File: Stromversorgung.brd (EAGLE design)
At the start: 70 x 100 mm, 17 parts, among them IC1 LM2574N-3.3, X1 MSTBV4, X2 Power ext., 5V 1A, X4 Power int., 5V 3A

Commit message: Pi und Stromversorgung Rev. 2019
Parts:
- removed C1: 22µF 75V, rcl:E2,5-5
- removed C2: 220µF 25V, rcl:E2,5-5
- removed D1: 1N5819-B, diode:DO41-7.6
- removed IC1: LM2574N-3.3, linear:DIL08
- removed L1: 100µH, rcl:6000-XXXX-RC
- removed SV1: PLATINENVERBINDER-31SMD, homepi:PLATINENVERBINDER-31-SMD
- removed X4: Power int., 5V 3A, con-phoenix-508:MSTBV2
- added J1: DCJ0202, con-jack:DCJ0202
- added U1, U3: TSR_2-2450, _traco_tsr-1:TSR-1
- added U2: TSR_0.5-2433, _traco_tsr-1:TSR-1
- X1: value MSTBV4 -> Ein/Aus; device con-phoenix-508:MSTBV4 -> con-phoenix-508:MSTBV2
- X2: value Power ext., 5V 1A -> MAC64L; device con-phoenix-508:MSTBV2 -> con-vg:MAC64L
- moved X2 65.0 mm to (2.54, 50.0), turned to 180 degrees
- moved R2 50.8 mm to (53.3, 63.5)
- moved JP2 45.6 mm to (45.7, 63.5), turned to 90 degrees
- moved LED2 43.2 mm to (59.7, 62.2), turned to 270 degrees
- moved R1 38.1 mm to (53.3, 47.0)
- moved LED1 35.6 mm to (59.7, 45.7), turned to 270 degrees
- moved X1 31.1 mm to (58.4, 28.6)
- moved JP1 23.3 mm to (45.7, 58.4), turned to 270 degrees
- moved LED3 16.6 mm to (59.7, 77.5), turned to 270 degrees
- moved R3 14.0 mm to (53.3, 78.7)
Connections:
- removed net +3,3V_INT_1: C2.+, IC1.1, JP2.2, L1.1
- removed net GND_EXT: LED3.K, SV1.30, SV1.30T, X2.1
- removed net GND_INT: C1.-, C2.-, D1.A, IC1.2, IC1.3, IC1.4, LED1.K, LED2.K, SV1.29, SV1.29T, SV1.3, SV1.3T, SV1.6, SV1.6T, SV1.8, SV1.8T, X4.1
- removed net LM2574_IN: C1.+, IC1.5, JP1.1
- removed net LM2574_OUT: D1.C, IC1.7, L1.2
- removed net N$3: X1.3, X4.2
- new net +24V: JP1.2, U1.1, U3.1, X1.1, X2.A32, X2.C32
- new net GND: J1.3, LED1.K, LED2.K, LED3.K, U1.2, U2.2, U3.2, X2.A29, X2.A3, X2.A30, X2.A6, X2.A8, X2.C29, X2.C3, X2.C30, X2.C6, X2.C8
- new net N$2: JP2.2, U2.3
- new net VI: JP1.1, U2.1
- net +3,3V: now also X2.A2, X2.C2; no longer SV1.2, SV1.2T
- net +5V_EXT: now also U3.3, X2.A31, X2.C31; no longer SV1.31, SV1.31T, X1.2
- net +5V_INT: now also U1.3, X2.A1, X2.A28, X2.C1, X2.C28; no longer JP1.2, SV1.1, SV1.1T, SV1.28, SV1.28T, X1.4
- net N$1: now also J1.1, X1.2; no longer X1.1, X2.2
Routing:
- net GND: track 0.00 -> 309.6 mm
- net GND_INT: track 179.1 -> 0.00 mm
- net +24V: track 0.00 -> 141.2 mm
- net N$4: track 102.9 -> 0.00 mm
- net +5V_INT: track 229.0 -> 148.9 mm, vias 2 -> 1
- net GND_EXT: track 73.1 -> 0.00 mm
- net +5V_EXT: track 108.1 -> 53.8 mm, vias 1 -> 0
- net +3,3V: track 51.6 -> 92.8 mm
- net N$3: track 31.6 -> 0.00 mm
- net LM2574_IN: track 18.8 -> 0.00 mm
- net N$7: track 6.66 -> 0.00 mm
- net VI: track 0.00 -> 6.35 mm
- net N$2: track 0.00 -> 6.35 mm
- net N$1: track 19.5 -> 20.6 mm
- added copper zone on layer 16, net GND
- removed copper zone on layer 16, net +3,3V_INT_1
- removed copper zone on layer 16, net GND_INT
- removed copper zone on layer 16, net LM2574_OUT
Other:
- board text added: "+24V Eingang"
- board text added: "+3,3V"
- board text added: "HomePi Stromversorgung Rev 2019/03 (c) Peter Müller"
- board text removed: "+3,3V i.O."
- board text removed: "+5V i.O."
- board text removed: "Erzeug. +3,3V"
- board text removed: "HomePi Stromversorgung Rev 2015/12 (c) Peter Müller"

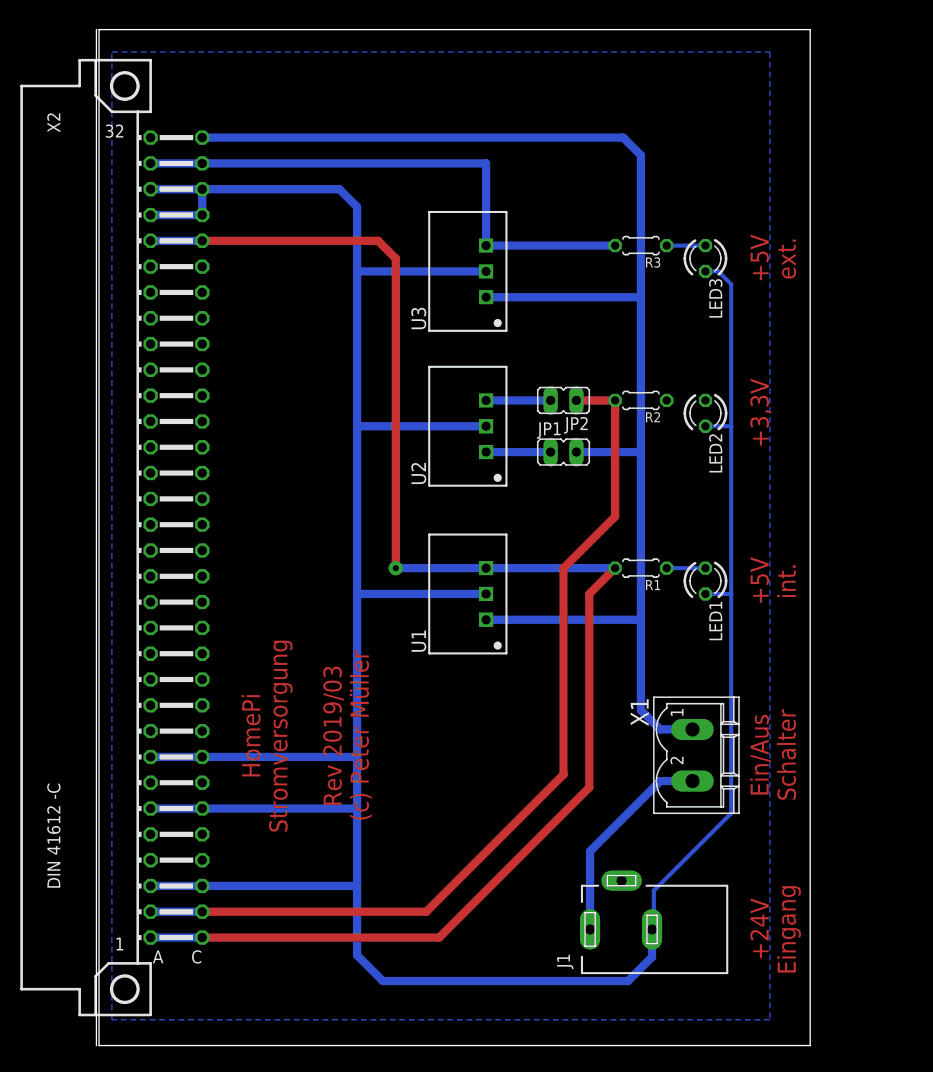
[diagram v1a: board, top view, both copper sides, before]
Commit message: Anpassungen an Rev. 2019, erste Can-Bus Elemente
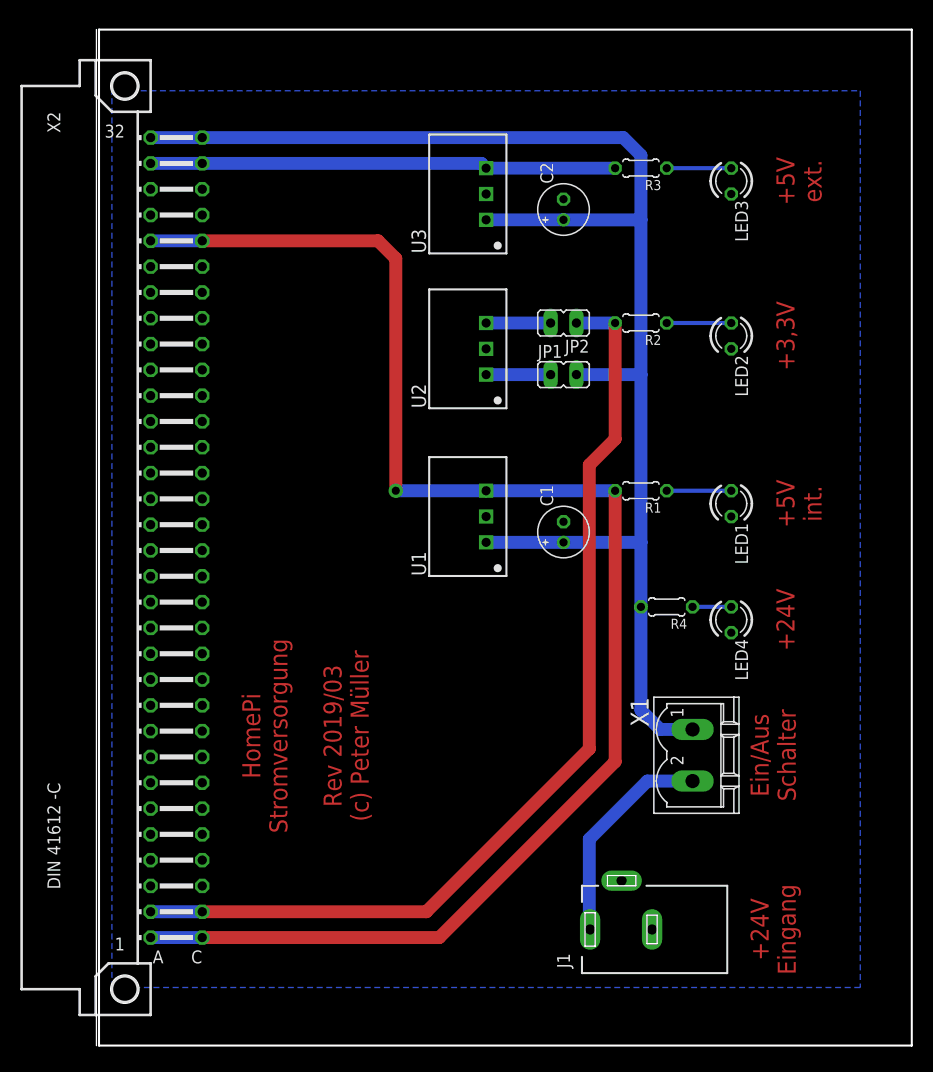
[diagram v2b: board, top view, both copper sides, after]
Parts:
- added C1, C2: 22µF/50V, rcl:E2-5
- added LED4: 2mA ge, led:LED3MM
- added R4: 12k, rcl:0204/5
- U1, U3: value TSR_2-2450 -> TSR 2-2450
- U2: value TSR_0.5-2433 -> TSR 1-2433
- moved LED1 8.03 mm to (62.2, 53.3)
- moved LED3 8.03 mm to (62.2, 85.1)
- moved LED2 8.03 mm to (62.2, 69.8)
- moved JP1 7.62 mm to (45.7, 66.0)
- moved JP2 7.62 mm to (45.7, 71.1)
- moved R2 7.62 mm to (53.3, 71.1)
- moved R3 7.62 mm to (53.3, 86.4)
- moved R1 7.62 mm to (53.3, 54.6)
- moved U1 7.62 mm to (38.1, 52.1)
- moved U2 7.62 mm to (38.1, 68.6)
- moved U3 7.62 mm to (38.1, 83.8)
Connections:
- new net N$3: LED4.A, R4.1
- net +24V: now also C1.+, C2.+, R4.2
- net GND: now also C1.-, C2.-, LED4.K
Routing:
- net GND: track 309.6 -> 0.00 mm
- net +5V_EXT: track 53.8 -> 45.9 mm
- net N$7: track 0.00 -> 6.35 mm
- net +24V: track 141.2 -> 146.3 mm
- net +3,3V: track 92.8 -> 96.6 mm
- net N$3: track 0.00 -> 3.81 mm
- net N$8: track 3.81 -> 6.35 mm
- net N$6: track 3.81 -> 6.35 mm
- net N$1: track 20.6 -> 21.4 mm
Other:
- board size 70 x 100 mm -> 80 x 100 mm
- board text added: "+24V"

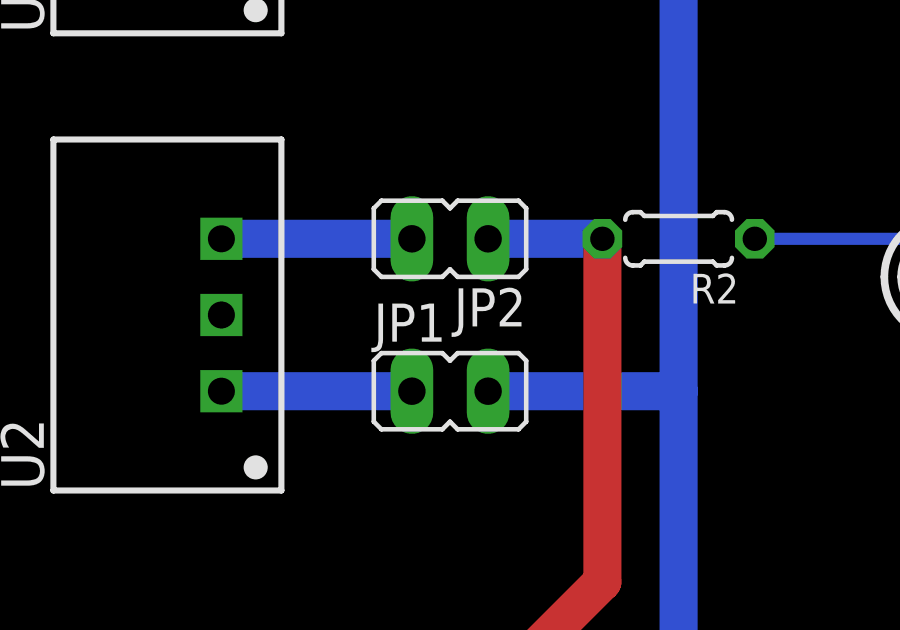
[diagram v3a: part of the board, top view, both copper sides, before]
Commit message: 3,3V-Versorgung nur noch über TSR-Spannungsregler
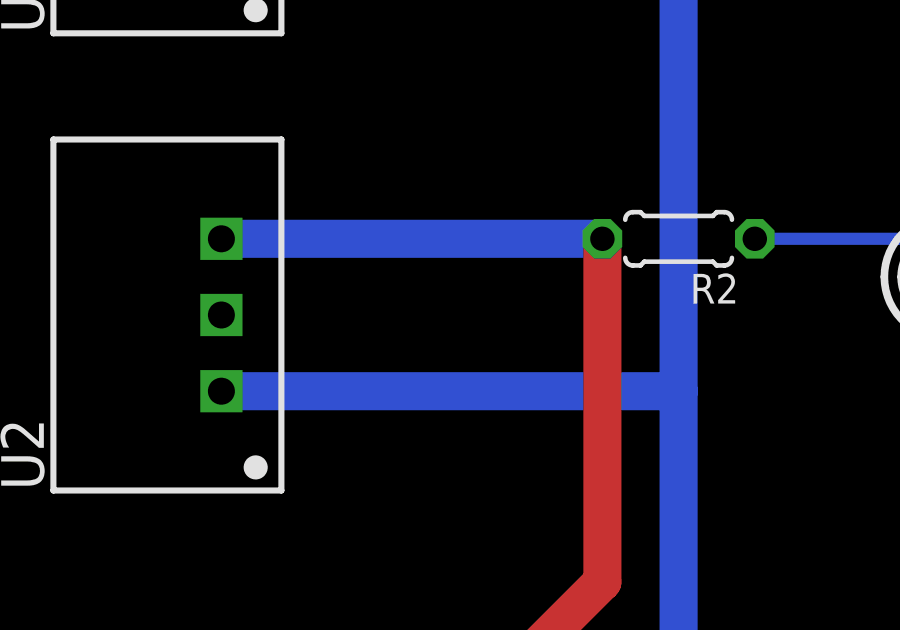
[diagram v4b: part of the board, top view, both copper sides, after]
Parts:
- removed JP1, JP2: (no value), jumper:JP1
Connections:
- removed net N$2: JP2.2, U2.3
- removed net VI: JP1.1, U2.1
- net +24V: now also U2.1; no longer JP1.2
- net +3,3V: now also U2.3; no longer JP2.1
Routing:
- net +3,3V: track 96.6 -> 105.5 mm
- net +24V: track 146.3 -> 155.2 mm
- net VI: track 6.35 -> 0.00 mm
- net N$2: track 6.35 -> 0.00 mm
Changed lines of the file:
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@@
 </autorouter>
 <elements>
-<element name="JP1" library="jumper" package="JP1" value="" x="45.72" y="66.04" rot="R270"/>
-<element name="JP2" library="jumper" package="JP1" value="" x="45.72" y="71.12" rot="R90"/>
 <element name="X1" library="con-phoenix-508" package="MSTBV2" value="Ein/Aus" x="58.42" y="28.575" rot="R270">
 <attribute name="OC_NEWARK" value="69R9845" x="58.42" y="28.575" size="1.778" layer="27" rot="R270" display="off"/>
@@
 </signal>
 <signal name="+3,3V">
-<contactref element="JP2" pad="1"/>
 <contactref element="R2" pad="2"/>
 <contactref element="X2" pad="A2"/>
@@
 <wire x1="48.26" y1="57.15" x2="48.26" y2="29.21" width="1.27" layer="1"/>
 <wire x1="10.16" y1="13.17" x2="5.08" y2="13.17" width="1.27" layer="16"/>
-<wire x1="46.99" y1="71.12" x2="50.8" y2="71.12" width="1.27" layer="16"/>
+<contactref element="U2" pad="3"/>
+<wire x1="38.1" y1="71.12" x2="50.8" y2="71.12" width="1.27" layer="16"/>
 </signal>
 <signal name="N$6">
@@
 <signal name="N$4">
 </signal>
-<signal name="N$2">
-<contactref element="U2" pad="3"/>
-<contactref element="JP2" pad="2"/>
-<wire x1="44.45" y1="71.12" x2="38.1" y2="71.12" width="1.27" layer="16"/>
-</signal>
-<signal name="VI">
-<contactref element="JP1" pad="1"/>
-<contactref element="U2" pad="1"/>
-<wire x1="44.45" y1="66.04" x2="38.1" y2="66.04" width="1.27" layer="16"/>
-</signal>
 <signal name="+24V">
-<contactref element="JP1" pad="2"/>
 <contactref element="U1" pad="1"/>
 <contactref element="U3" pad="1"/>
@@
 <wire x1="51.6" y1="89.37" x2="53.34" y2="87.63" width="1.27" layer="16"/>
 <contactref element="X1" pad="1"/>
-<wire x1="46.99" y1="66.04" x2="53.34" y2="66.04" width="1.27" layer="16"/>
 <wire x1="58.42" y1="31.115" x2="55.245" y2="31.115" width="1.27" layer="16"/>
 <wire x1="55.245" y1="31.115" x2="53.34" y2="33.02" width="1.27" layer="16"/>
@@
 <wire x1="53.34" y1="49.529" x2="53.34" y2="43.18" width="1.27" layer="16"/>
 <wire x1="53.34" y1="43.18" x2="53.34" y2="33.02" width="1.27" layer="16"/>
+<contactref element="U2" pad="1"/>
+<wire x1="38.1" y1="66.04" x2="53.34" y2="66.04" width="1.27" layer="16"/>
 </signal>
 <signal name="GND">

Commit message: 1-Wire Sensor auf Raspi-Platine
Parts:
- C1, C2: value 22µF/50V -> 22µF 50V Low-ESR
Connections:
- new net +5V_1WIRE: X2.C7
- new net 1WIRE: X2.A7
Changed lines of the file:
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@@
 </element>
 <element name="X2" library="con-vg" package="MAC64L" value="MAC64L" x="2.54" y="50" rot="R180"/>
-<element name="C1" library="rcl" package="E2-5" value="22µF/50V" x="45.72" y="50.545" rot="R90"/>
-<element name="C2" library="rcl" package="E2-5" value="22µF/50V" x="45.72" y="82.292" rot="R90"/>
+<element name="C1" library="rcl" package="E2-5" value="22µF 50V Low-ESR" x="45.72" y="50.545" rot="R90"/>
+<element name="C2" library="rcl" package="E2-5" value="22µF 50V Low-ESR" x="45.72" y="82.292" rot="R90"/>
 <element name="R4" library="rcl" package="0204/5" value="12k" x="55.88" y="43.18" rot="R180"/>
 <element name="LED4" library="led" package="LED3MM" value="2mA ge" x="62.23" y="41.91" rot="R270"/>
@@
 <wire x1="58.42" y1="43.18" x2="62.23" y2="43.18" width="0.4064" layer="16"/>
 </signal>
+<signal name="+5V_1WIRE">
+<contactref element="X2" pad="C7"/>
+</signal>
+<signal name="1WIRE">
+<contactref element="X2" pad="A7"/>
+</signal>
 </signals>

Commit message: Diverse Anpassungen
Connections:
- net +5V_1WIRE renamed !PI_RESET
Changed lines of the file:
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@@
 <wire x1="58.42" y1="43.18" x2="62.23" y2="43.18" width="0.4064" layer="16"/>
 </signal>
-<signal name="+5V_1WIRE">
+<signal name="!PI_RESET">
 <contactref element="X2" pad="C7"/>
 </signal>
